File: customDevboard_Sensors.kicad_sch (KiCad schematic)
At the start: 17 parts, among them U1 DPS310, U7 BMI270

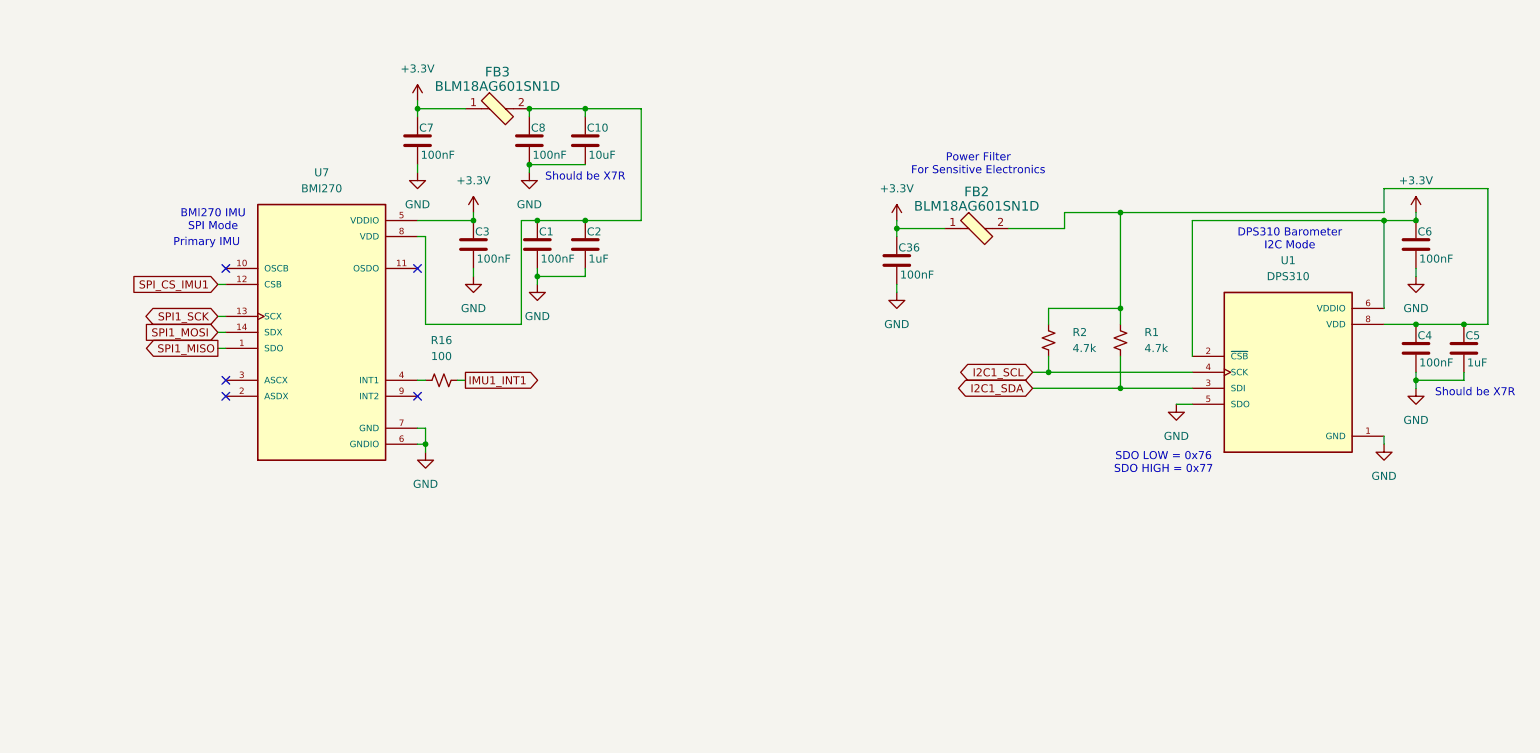
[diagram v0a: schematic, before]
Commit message: switch imu and barometer
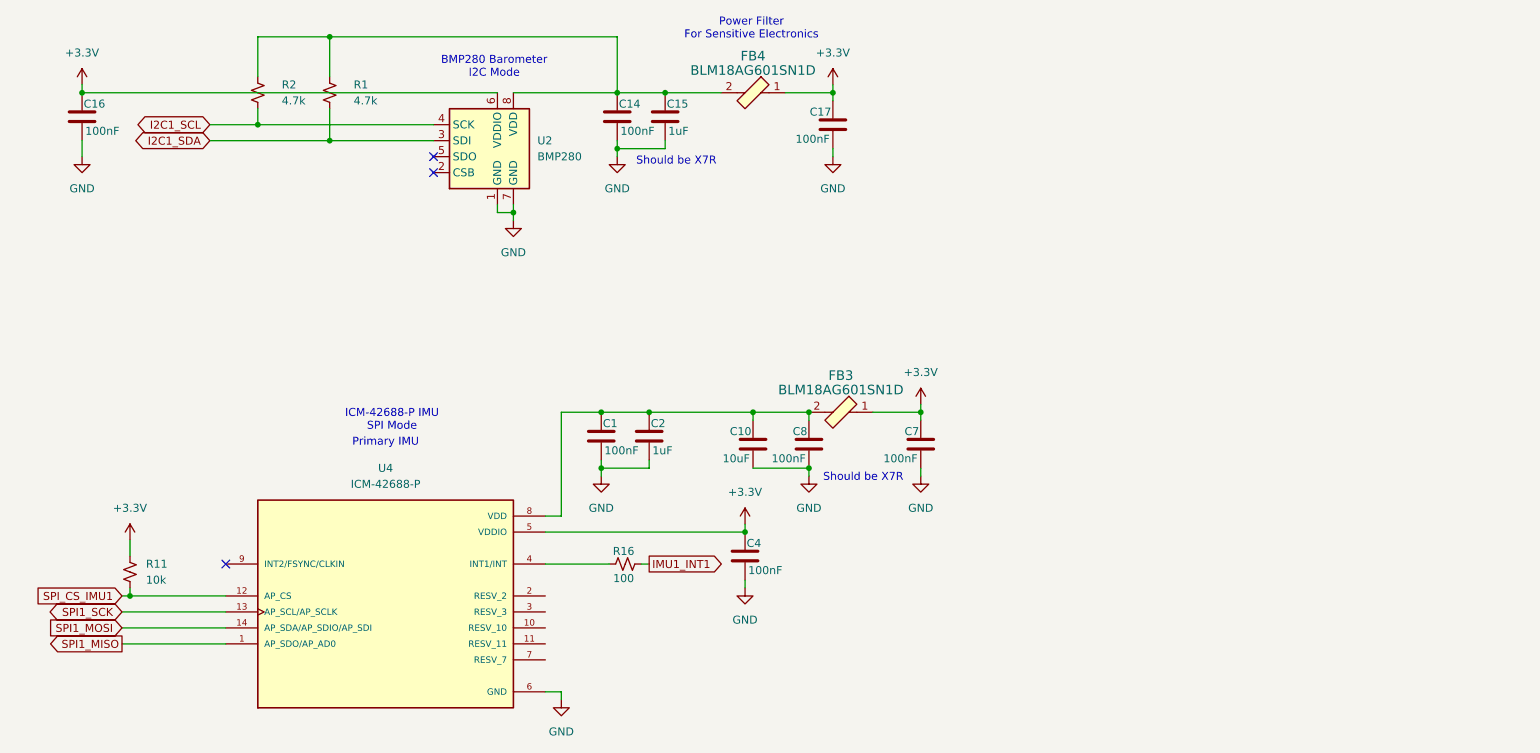
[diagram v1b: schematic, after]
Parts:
- removed C3, C6: 100nF, Capacitor_SMD:C_0402_1005Metric_Pad0.74x0.62mm_HandSolder, symbol Device:C
- removed C36: 100nF, Capacitor_SMD:C_0603_1608Metric_Pad1.08x0.95mm_HandSolder, symbol Device:C
- removed C5: 1uF, Capacitor_SMD:C_0402_1005Metric_Pad0.74x0.62mm_HandSolder, symbol Device:C
- removed FB2: BLM18AG601SN1D, digikey-footprints:0603, symbol dk_Ferrite-Beads-and-Chips:BLM18AG601SN1D
- removed U1: DPS310, DPS310:XDCR_DPS310, symbol DPS310:DPS310
- removed U7: BMI270, BMI270:XDCR_BMI270, symbol BMI270:BMI270
- added C14, C16: 100nF, Capacitor_SMD:C_0402_1005Metric_Pad0.74x0.62mm_HandSolder, symbol Device:C
- added C15: 1uF, Capacitor_SMD:C_0402_1005Metric_Pad0.74x0.62mm_HandSolder, symbol Device:C
- added C17: 100nF, Capacitor_SMD:C_0603_1608Metric_Pad1.08x0.95mm_HandSolder, symbol Device:C
- added FB4: BLM18AG601SN1D, digikey-footprints:0603, symbol dk_Ferrite-Beads-and-Chips:BLM18AG601SN1D
- added R11: 10k, Resistor_SMD:R_0603_1608Metric_Pad0.98x0.95mm_HandSolder, symbol Device:R_Small_US
- added U2: BMP280, Package_LGA:Bosch_LGA-8_2x2.5mm_P0.65mm_ClockwisePinNumbering, symbol Sensor_Pressure:BMP280
- added U4: ICM-42688-P, ICM_42688_P:PQFN50P300X250X97-14N, symbol ICM-42688-P:ICM-42688-P
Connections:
- net +3.3V: now also C4.1, C16.1, C17.1, FB4.1, R11.2, U2.6 (VDDIO), U4.5 (VDDIO)
- net GND: now also C14.2, C15.2, C16.2, C17.2, U2.1 (GND), U2.7 (GND), U4.6 (GND)
- net I2C1_SCL: now also U2.4 (SCK)
- net I2C1_SDA: now also U2.3 (SDI)
- net SPI1_MISO: now also U4.1 (AP_SDO/AP_AD0)
- net SPI1_MOSI: now also U4.14 (AP_SDA/AP_SDIO/AP_SDI)
- net SPI1_SCK: now also U4.13 (AP_SCL/AP_SCLK)
- net SPI_CS_IMU1: now also R11.1, U4.12 (AP_CS)
- net at C1.1, C10.1, C2.1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: now also U4.8 (VDD)
- net at R1.1, R2.1: now also C14.1, C15.1, FB4.2, U2.8 (VDD); no longer C4.1
- net at R16.1: now also U4.4 (INT1/INT)
- no-connect marks 5 -> 3
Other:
- note added: "BMP280 Barometer I2C Mode"
- note added: "ICM-42688-P IMU SPI Mode"
- note removed: "BMI270 IMU SPI Mode"
- note removed: "DPS310 Barometer I2C Mode"
- note removed: "SDO LOW = 0x76 SDO HIGH = 0x77"
- moved on the sheet: C1, C10, C2, C7, C8, FB3, R1, R16, R2

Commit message: restart pcb because too many new parts
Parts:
- renumbered C16 to C17, C1 to C18, C14 to C19, C2 to C20, C15 to C21, C4 to C22, C10 to C23, C8 to C24, C17 to C25, C7 to C26, FB4 to FB2, R11 to R13, R2 to R14, R1 to R15, U2 to U5
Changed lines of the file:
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@@
 		(on_board yes)
 		(dnp no)
-		(property "Reference" "C10"
+		(property "Reference" "C23"
 			(at 140.716 86.868 0)
 			(effects
@@
 			(project "customDevboard"
 				(path "/87078d80-bd64-4f8e-8d0b-a79df4010aa3/36a94c75-36a8-448f-a6ca-e345a534184d"
-					(reference "C10")
+					(reference "C23")
 					(unit 1)
 				)
@@
 		(dnp no)
 		(fields_autoplaced yes)
-		(property "Reference" "#PWR047"
+		(property "Reference" "#PWR040"
 			(at 119.38 49.53 0)
 			(effects
@@
 			(project "customDevboard"
 				(path "/87078d80-bd64-4f8e-8d0b-a79df4010aa3/36a94c75-36a8-448f-a6ca-e345a534184d"
-					(reference "#PWR047")
+					(reference "#PWR040")
 					(unit 1)
 				)
@@
 		(on_board yes)
 		(dnp no)
-		(property "Reference" "C14"
+		(property "Reference" "C19"
 			(at 119.634 34.798 0)
 			(effects
@@
 			(project "customDevboard"
 				(path "/87078d80-bd64-4f8e-8d0b-a79df4010aa3/36a94c75-36a8-448f-a6ca-e345a534184d"
-					(reference "C14")
+					(reference "C19")
 					(unit 1)
 				)
@@
 		(dnp no)
 		(fields_autoplaced yes)
-		(property "Reference" "R2"
+		(property "Reference" "R14"
 			(at 66.04 31.7499 0)
 			(effects
@@
 			(project "customDevboard"
 				(path "/87078d80-bd64-4f8e-8d0b-a79df4010aa3/36a94c75-36a8-448f-a6ca-e345a534184d"
-					(reference "R2")
+					(reference "R14")
 					(unit 1)
 				)
@@
 		(on_board yes)
 		(dnp no)
-		(property "Reference" "C7"
+		(property "Reference" "C26"
 			(at 167.386 86.868 0)
 			(effects
@@
 			(project "customDevboard"
 				(path "/87078d80-bd64-4f8e-8d0b-a79df4010aa3/36a94c75-36a8-448f-a6ca-e345a534184d"
-					(reference "C7")
+					(reference "C26")
 					(unit 1)
 				)
@@
 		(on_board yes)
 		(dnp no)
-		(property "Reference" "FB4"
+		(property "Reference" "FB2"
 			(at 140.97 27.178 0)
 			(effects
@@
 			(project "customDevboard"
 				(path "/87078d80-bd64-4f8e-8d0b-a79df4010aa3/36a94c75-36a8-448f-a6ca-e345a534184d"
-					(reference "FB4")
+					(reference "FB2")
 					(unit 1)
 				)
@@
 		(dnp no)
 		(fields_autoplaced yes)
-		(property "Reference" "#PWR023"
+		(property "Reference" "#PWR046"
 			(at 167.64 86.36 0)
 			(effects
@@
 			(project "customDevboard"
 				(path "/87078d80-bd64-4f8e-8d0b-a79df4010aa3/36a94c75-36a8-448f-a6ca-e345a534184d"
-					(reference "#PWR023")
+					(reference "#PWR046")
 					(unit 1)
 				)
@@
 		(on_board yes)
 		(dnp no)
-		(property "Reference" "#PWR045"
+		(property "Reference" "#PWR038"
 			(at 110.49 135.89 0)
 			(effects
@@
 			(project "customDevboard"
 				(path "/87078d80-bd64-4f8e-8d0b-a79df4010aa3/36a94c75-36a8-448f-a6ca-e345a534184d"
-					(reference "#PWR045")
+					(reference "#PWR038")
 					(unit 1)
 				)
@@
 		(dnp no)
 		(fields_autoplaced yes)
-		(property "Reference" "#PWR024"
+		(property "Reference" "#PWR047"
 			(at 167.64 100.33 0)
 			(effects
@@
 			(project "customDevboard"
 				(path "/87078d80-bd64-4f8e-8d0b-a79df4010aa3/36a94c75-36a8-448f-a6ca-e345a534184d"
-					(reference "#PWR024")
+					(reference "#PWR047")
 					(unit 1)
 				)
@@
 		(dnp no)
 		(fields_autoplaced yes)
-		(property "Reference" "R1"
+		(property "Reference" "R15"
 			(at 77.47 31.7499 0)
 			(effects
@@
 			(project "customDevboard"
 				(path "/87078d80-bd64-4f8e-8d0b-a79df4010aa3/36a94c75-36a8-448f-a6ca-e345a534184d"
-					(reference "R1")
+					(reference "R15")
 					(unit 1)
 				)
@@
 		(dnp no)
 		(fields_autoplaced yes)
-		(property "Reference" "#PWR051"
+		(property "Reference" "#PWR045"
 			(at 153.67 49.53 0)
 			(effects
@@
 			(project "customDevboard"
 				(path "/87078d80-bd64-4f8e-8d0b-a79df4010aa3/36a94c75-36a8-448f-a6ca-e345a534184d"
-					(reference "#PWR051")
+					(reference "#PWR045")
 					(unit 1)
 				)
@@
 		(dnp no)
 		(fields_autoplaced yes)
-		(property "Reference" "#PWR048"
+		(property "Reference" "#PWR035"
 			(at 34.29 49.53 0)
 			(effects
@@
 			(project "customDevboard"
 				(path "/87078d80-bd64-4f8e-8d0b-a79df4010aa3/36a94c75-36a8-448f-a6ca-e345a534184d"
-					(reference "#PWR048")
+					(reference "#PWR035")
 					(unit 1)
 				)
@@
 		(on_board yes)
 		(dnp no)
-		(property "Reference" "C4"
+		(property "Reference" "C22"
 			(at 139.954 104.648 0)
 			(effects
@@
 			(project "customDevboard"
 				(path "/87078d80-bd64-4f8e-8d0b-a79df4010aa3/36a94c75-36a8-448f-a6ca-e345a534184d"
-					(reference "C4")
+					(reference "C22")
 					(unit 1)
 				)
@@
 		(dnp no)
 		(fields_autoplaced yes)
-		(property "Reference" "#PWR046"
+		(property "Reference" "#PWR037"
 			(at 102.87 59.69 0)
 			(effects
@@
 			(project "customDevboard"
 				(path "/87078d80-bd64-4f8e-8d0b-a79df4010aa3/36a94c75-36a8-448f-a6ca-e345a534184d"
-					(reference "#PWR046")
+					(reference "#PWR037")
 					(unit 1)
 				)
@@
 		(dnp no)
 		(fields_autoplaced yes)
-		(property "Reference" "#PWR01"
+		(property "Reference" "#PWR041"
 			(at 139.7 105.41 0)
 			(effects
@@
 			(project "customDevboard"
 				(path "/87078d80-bd64-4f8e-8d0b-a79df4010aa3/36a94c75-36a8-448f-a6ca-e345a534184d"
-					(reference "#PWR01")
+					(reference "#PWR041")
 					(unit 1)
 				)
@@
 		(dnp no)
 		(fields_autoplaced yes)
-		(property "Reference" "R11"
+		(property "Reference" "R13"
 			(at 44.45 107.9499 0)
 			(effects
@@
 			(project "customDevboard"
 				(path "/87078d80-bd64-4f8e-8d0b-a79df4010aa3/36a94c75-36a8-448f-a6ca-e345a534184d"
-					(reference "R11")
+					(reference "R13")
 					(unit 1)
 				)
@@
 		(dnp no)
 		(fields_autoplaced yes)
-		(property "Reference" "#PWR07"
+		(property "Reference" "#PWR039"
 			(at 116.84 100.33 0)
 			(effects
@@
 			(project "customDevboard"
 				(path "/87078d80-bd64-4f8e-8d0b-a79df4010aa3/36a94c75-36a8-448f-a6ca-e345a534184d"
-					(reference "#PWR07")
+					(reference "#PWR039")
 					(unit 1)
 				)
@@
 		(on_board yes)
 		(dnp no)
-		(property "Reference" "C16"
+		(property "Reference" "C17"
 			(at 34.544 34.798 0)
 			(effects
@@
 			(project "customDevboard"
 				(path "/87078d80-bd64-4f8e-8d0b-a79df4010aa3/36a94c75-36a8-448f-a6ca-e345a534184d"
-					(reference "C16")
+					(reference "C17")
 					(unit 1)
 				)
@@
 		(on_board yes)
 		(dnp no)
-		(property "Reference" "C17"
+		(property "Reference" "C25"
 			(at 153.416 36.068 0)
 			(effects
@@
 			(project "customDevboard"
 				(path "/87078d80-bd64-4f8e-8d0b-a79df4010aa3/36a94c75-36a8-448f-a6ca-e345a534184d"
-					(reference "C17")
+					(reference "C25")
 					(unit 1)
 				)
@@
 		(dnp no)
 		(fields_autoplaced yes)
-		(property "Reference" "#PWR06"
+		(property "Reference" "#PWR036"
 			(at 41.91 107.95 0)
 			(effects
@@
 			(project "customDevboard"
 				(path "/87078d80-bd64-4f8e-8d0b-a79df4010aa3/36a94c75-36a8-448f-a6ca-e345a534184d"
-					(reference "#PWR06")
+					(reference "#PWR036")
 					(unit 1)
 				)
@@
 		(on_board yes)
 		(dnp no)
-		(property "Reference" "C8"
+		(property "Reference" "C24"
 			(at 149.606 86.868 0)
 			(effects
@@
 			(project "customDevboard"
 				(path "/87078d80-bd64-4f8e-8d0b-a79df4010aa3/36a94c75-36a8-448f-a6ca-e345a534184d"
-					(reference "C8")
+					(reference "C24")
 					(unit 1)
 				)
@@
 		(on_board yes)
 		(dnp no)
-		(property "Reference" "C1"
+		(property "Reference" "C18"
 			(at 117.094 85.598 0)
 			(effects
@@
 			(project "customDevboard"
 				(path "/87078d80-bd64-4f8e-8d0b-a79df4010aa3/36a94c75-36a8-448f-a6ca-e345a534184d"
-					(reference "C1")
+					(reference "C18")
 					(unit 1)
 				)
@@
 		(on_board yes)
 		(dnp no)
-		(property "Reference" "C2"
+		(property "Reference" "C20"
 			(at 124.714 85.598 0)
 			(effects
@@
 			(project "customDevboard"
 				(path "/87078d80-bd64-4f8e-8d0b-a79df4010aa3/36a94c75-36a8-448f-a6ca-e345a534184d"
-					(reference "C2")
+					(reference "C20")
 					(unit 1)
 				)
@@
 		(dnp no)
 		(fields_autoplaced yes)
-		(property "Reference" "#PWR049"
+		(property "Reference" "#PWR034"
 			(at 34.29 35.56 0)
 			(effects
@@
 			(project "customDevboard"
 				(path "/87078d80-bd64-4f8e-8d0b-a79df4010aa3/36a94c75-36a8-448f-a6ca-e345a534184d"
-					(reference "#PWR049")
+					(reference "#PWR034")
 					(unit 1)
 				)
@@
 		(on_board yes)
 		(dnp no)
-		(property "Reference" "C15"
+		(property "Reference" "C21"
 			(at 127.254 34.798 0)
 			(effects
@@
 			(project "customDevboard"
 				(path "/87078d80-bd64-4f8e-8d0b-a79df4010aa3/36a94c75-36a8-448f-a6ca-e345a534184d"
-					(reference "C15")
+					(reference "C21")
 					(unit 1)
 				)
@@
 		(dnp no)
 		(fields_autoplaced yes)
-		(property "Reference" "#PWR029"
+		(property "Reference" "#PWR043"
 			(at 149.86 100.33 0)
 			(effects
@@
 			(project "customDevboard"
 				(path "/87078d80-bd64-4f8e-8d0b-a79df4010aa3/36a94c75-36a8-448f-a6ca-e345a534184d"
-					(reference "#PWR029")
+					(reference "#PWR043")
 					(unit 1)
 				)
@@
 		(dnp no)
 		(fields_autoplaced yes)
-		(property "Reference" "#PWR050"
+		(property "Reference" "#PWR044"
 			(at 153.67 35.56 0)
 			(effects
@@
 			(project "customDevboard"
 				(path "/87078d80-bd64-4f8e-8d0b-a79df4010aa3/36a94c75-36a8-448f-a6ca-e345a534184d"
-					(reference "#PWR050")
+					(reference "#PWR044")
 					(unit 1)
 				)
@@
 		(dnp no)
 		(fields_autoplaced yes)
-		(property "Reference" "#PWR09"
+		(property "Reference" "#PWR042"
 			(at 139.7 118.11 0)
 			(effects
@@
 			(project "customDevboard"
 				(path "/87078d80-bd64-4f8e-8d0b-a79df4010aa3/36a94c75-36a8-448f-a6ca-e345a534184d"
-					(reference "#PWR09")
+					(reference "#PWR042")
 					(unit 1)
 				)
@@
 		(dnp no)
 		(fields_autoplaced yes)
-		(property "Reference" "U2"
+		(property "Reference" "U5"
 			(at 106.68 40.6399 0)
 			(effects
@@
 			(project ""
 				(path "/87078d80-bd64-4f8e-8d0b-a79df4010aa3/36a94c75-36a8-448f-a6ca-e345a534184d"
-					(reference "U2")
-					(unit 1)
-				)
+					(reference "U5")
+					(unit 1)
+				)

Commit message: add ground plane
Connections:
- no-connect marks 3 -> 8
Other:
- moved on the sheet: C22, C23, C24
